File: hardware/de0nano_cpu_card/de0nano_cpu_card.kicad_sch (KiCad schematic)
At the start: 0 parts

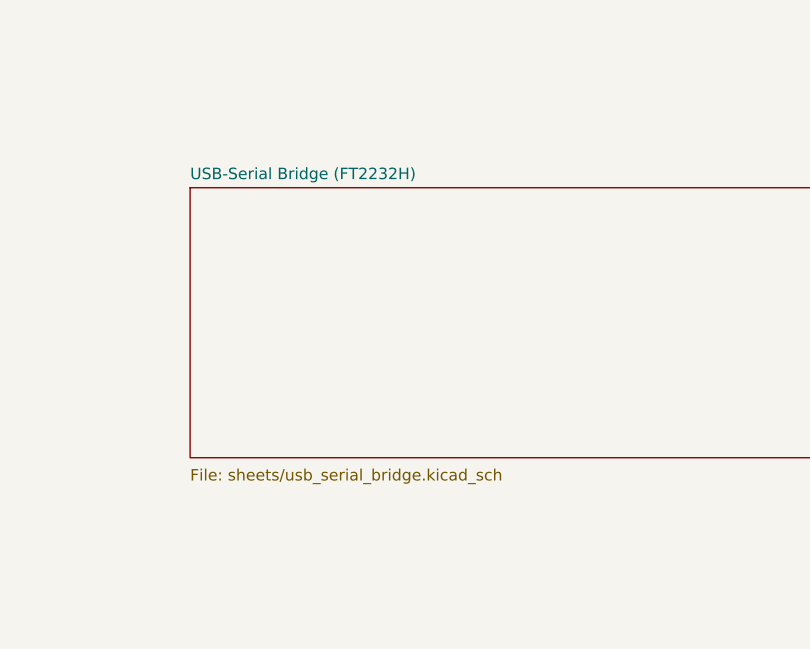
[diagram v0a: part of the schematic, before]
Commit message: Sync docs/schematic skeleton with FT2232H -> Raspberry Pi Pico-W decision
Pico-W replaces the FT2232H dual-UART bridge (cheaper, fast enough for
2 simple UARTs, adds WiFi/telnet and spare GPIOs for free). Renamed the
placeholder schematic sheet accordingly and updated design_notes.md to
reflect the now-resolved backplane pinout, Eurocard floorplan, and
front-panel wiring, plus the new open items the Pico-W swap introduces
(antenna keepout, USB/backplane back-feed protection).

Co-Authored-By: Claude Sonnet 5 <noreply@anthropic.com>
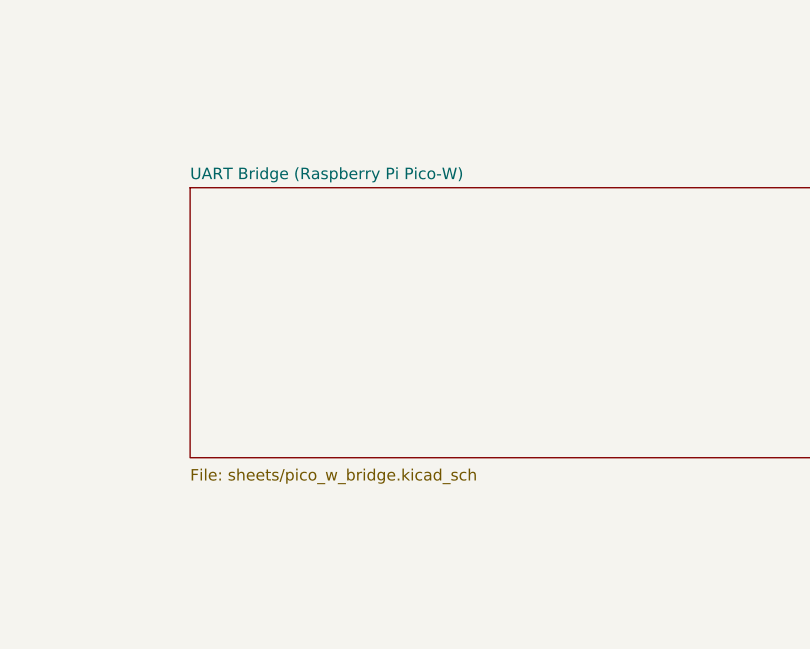
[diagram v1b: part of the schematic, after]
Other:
- sheet USB-Serial Bridge (FT2232H) renamed UART Bridge (Raspberry Pi Pico-W)
- sheet UART Bridge (Raspberry Pi Pico-W): file sheets/usb_serial_bridge.kicad_sch -> sheets/pico_w_bridge.kicad_sch
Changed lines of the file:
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@@
 			(color 0 0 0 0)
 		)
-		(property "Sheetname" "USB-Serial Bridge (FT2232H)"
+		(property "Sheetname" "UART Bridge (Raspberry Pi Pico-W)"
 			(at 120 99.2 0)
 			(show_name no)
@@
 			)
 		)
-		(property "Sheetfile" "sheets/usb_serial_bridge.kicad_sch"
+		(property "Sheetfile" "sheets/pico_w_bridge.kicad_sch"
 			(at 120 131.2 0)
 			(show_name no)
